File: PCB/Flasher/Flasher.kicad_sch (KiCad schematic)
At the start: 58 parts, among them J1 Reset, J2 Wago, J3 Wago, J4 USB-C-Socket-V, J5 TF_PUSH, U1 ESP32-S3-MINI-1, U2 TPS562246, U3 FT231XQ, U4 TPS22916CNYFPR

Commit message: Started placement
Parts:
- removed FID1, FID2: Fiducial, Fiducial:Fiducial_1mm_Mask2mm, symbol Mechanical:Fiducial
- removed V1, V4: ~, RevK:VCUT70N, symbol RevK:VCUT

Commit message: New tweaks
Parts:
- added D11: XL-1010RGBC-WS2812B, RevK:SMD1010, symbol RevK:WS2812B-1mm
- added U5: TPS22916CNYFPR, RevK:WCSP-4-0.78x0.78, symbol RevK:TPS22916
- C13: footprint RevK:C_0402 -> RevK:C_0201
- J2, J3: footprint RevK:WAGO-2060-453-998-404 -> RevK:WAGO-2060-453-998-404-S
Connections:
- net DC is gone; now on net VBUS: C1.1, C2.1, C3.1, R1.2, U2.1 (VIN)
- net +3.3V: now also D11.2 (+), U5.A2 (VIN)
- net GND: now also D11.3 (-), U5.B1 (GND)
- net LED: now also U1.16 (GPIO12); no longer U1.27 (GPIO47)
- net SDCD: now also U1.12 (GPIO8); no longer U1.22 (GPIO18)
- net SDCLK: now also U1.9 (GPIO5); no longer U1.19 (GPIO15)
- net SDCMD: now also U1.8 (GPIO4); no longer U1.18 (GPIO14)
- net SDDAT0: now also U1.10 (GPIO6); no longer U1.20 (GPIO16)
- net SDDAT1: now also U1.11 (GPIO7); no longer U1.21 (GPIO17)
- net SDDAT2: now also U1.6 (GPIO2); no longer U1.16 (GPIO12)
- net SDDAT3: now also U1.7 (GPIO3); no longer U1.17 (GPIO13)
- net at D10.1 (O): now also D11.4 (I)
- net VOUT: now reaches J3.1 (Pin_1), U4.A1 (VOUT)
- net VOUT: now also U5.A1 (VOUT)
- net PWR3: now reaches U1.13 (GPIO9)
- net PWR3: now also U5.B2 (ON)
- net PWR renamed PWR5
- no-connect marks 27 -> 26

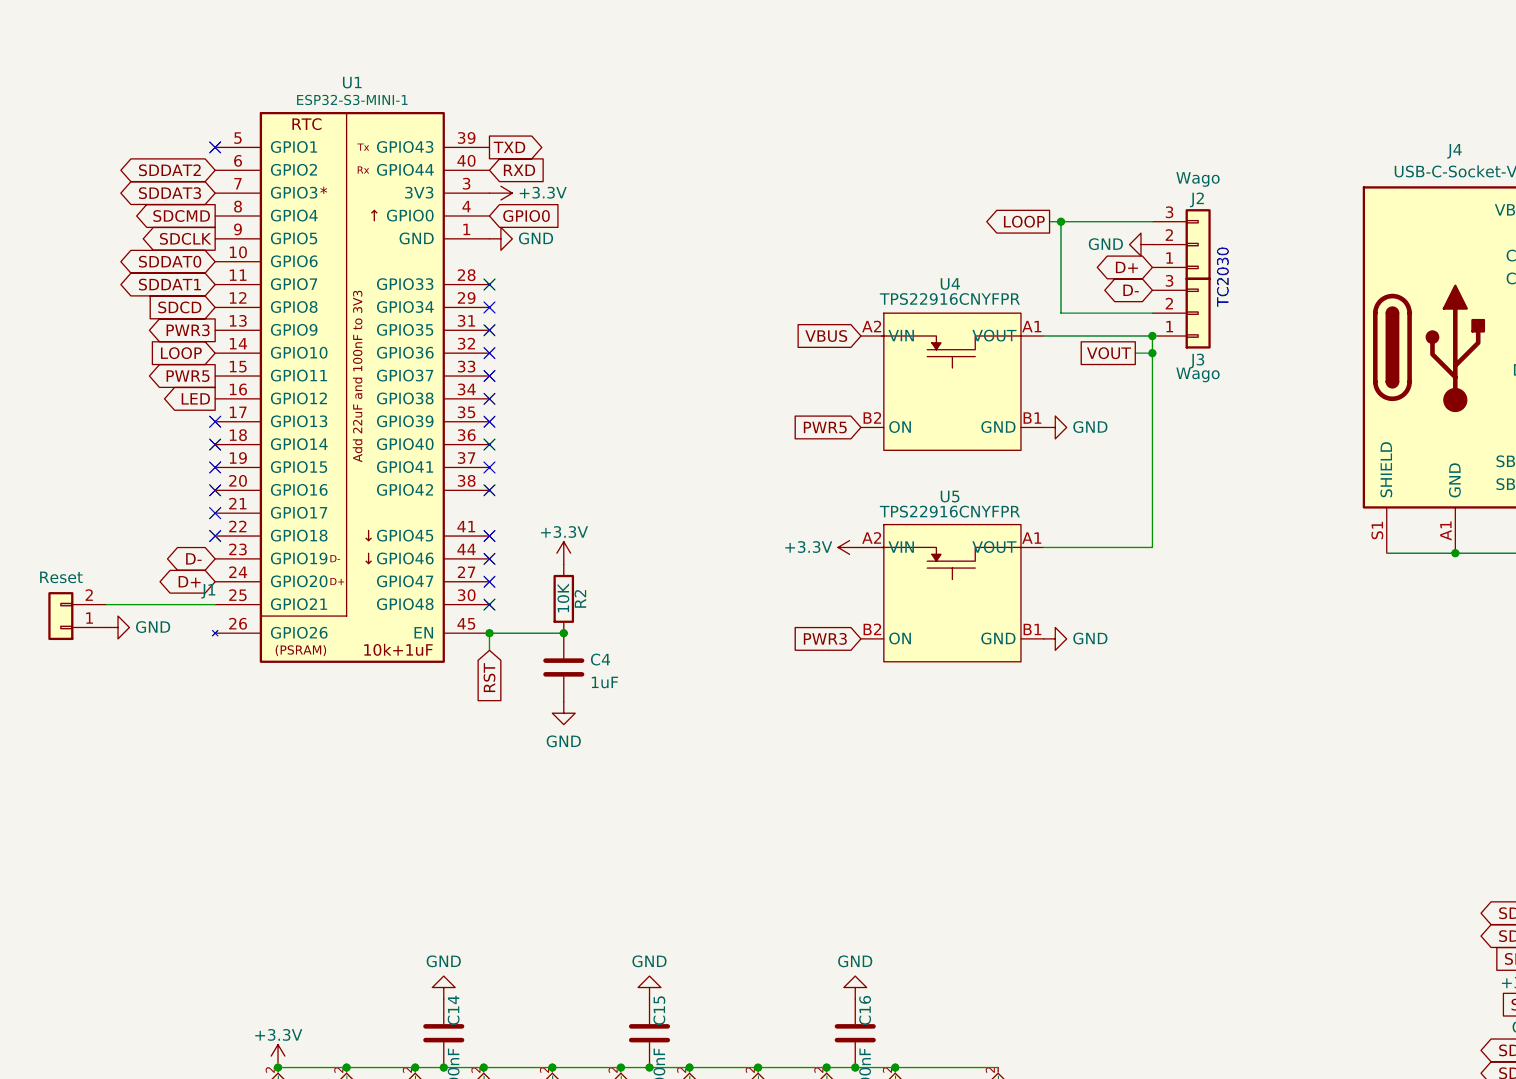
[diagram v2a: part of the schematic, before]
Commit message: New sockets
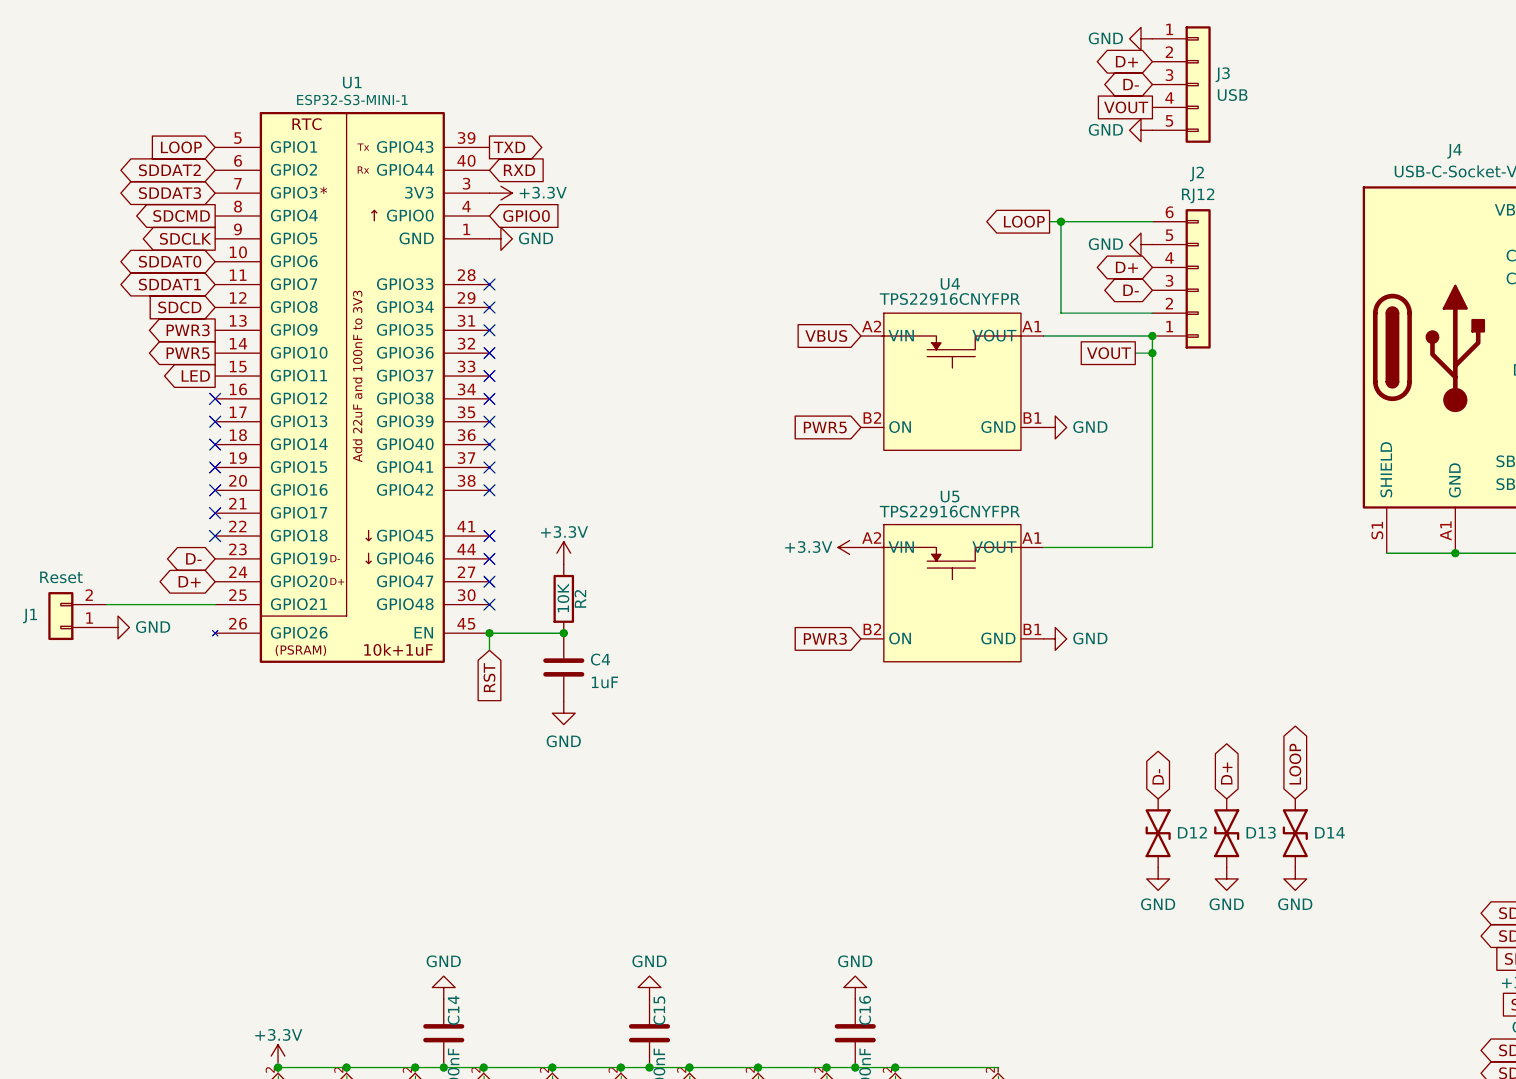
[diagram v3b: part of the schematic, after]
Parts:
- removed J2, J3: Wago, RevK:WAGO-2060-453-998-404-S, symbol Connector_Generic:Conn_01x03
- added D12, D13, D14: ~, RevK:DFN1006-2L, symbol RevK:ES05D1MC10
- added J2: RJ12, RevK:RJ12_Horizontal, symbol Connector_Generic:Conn_01x06
- added J3: USB, RevK:USB_A_Horizontal, symbol Connector_Generic:Conn_01x05
- R10, R9: MPN (none) -> C273295
- R7, R8: MPN (none) -> C270344
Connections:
- net D+: now also D13.2, J2.4 (Pin_4), J3.2 (Pin_2)
- net D-: now also D12.2, J2.3 (Pin_3), J3.3 (Pin_3)
- net GND: now also D12.1, D13.1, D14.1, J2.5 (Pin_5), J3.1 (Pin_1), J3.5 (Pin_5)
- net LED: now also U1.15 (GPIO11); no longer U1.16 (GPIO12)
- net LOOP: now also U1.5 (GPIO1), D14.2, J2.2 (Pin_2), J2.6 (Pin_6); no longer U1.14 (GPIO10)
- net PWR5: now also U1.14 (GPIO10); no longer U1.15 (GPIO11)
- net VOUT: now also J2.1 (Pin_1), J3.4 (Pin_4)
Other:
- note removed: "TC2030"

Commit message: Board ready
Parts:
- added SW1: SW_Push_DPDT, RevK:SW_Push_DPDT, symbol RevK:SW_Push_DPDT
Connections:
- net GND: now also SW1.3 (C)
- net BTN: now reaches U1.16 (GPIO12)
- net BTN: now also SW1.2 (B)
- no-connect marks 26 -> 29
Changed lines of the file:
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@@
 	)
 	(no_connect
+		(at 50.8 101.6)
+	)
+	(no_connect
 		(at 43.815 61.595)
 	)
@@
 	)
 	(no_connect
+		(at 60.96 101.6)
+	)
+	(no_connect
 		(at 43.815 64.135)
 	)
@@
 	)
 	(no_connect
-		(at 74.295 48.895)
+		(at 43.815 59.055)
 	)
 	(no_connect
-		(at 43.815 59.055)
+		(at 66.04 101.6)
 	)
 	(no_connect
@@
 	)
 	(no_connect
-		(at 43.815 56.515)
+		(at 74.295 48.895)
 	)
 	(no_connect
@@
 	)
 	(no_connect
+		(at 63.5 111.76)
+	)
+	(no_connect
 		(at 74.295 56.515)
 	)
@@
 		)
 	)
+	(global_label "BTN"
+		(shape input)
+		(at 43.815 56.515 180)
+		(fields_autoplaced yes)
+		(effects
+			(font
+				(size 1.27 1.27)
+			)
+			(justify right)
+		)
+		(property "Intersheetrefs" "${INTERSHEET_REFS}"
+			(at 37.9159 56.515 0)
+			(effects
+				(font
+					(size 1.27 1.27)
+				)
+				(justify right)
+				(hide yes)
+			)
+		)
+	)
 	(global_label "VOUT"
 		(shape passive)
@@
 		)
 	)
+	(global_label "BTN"
+		(shape output)
+		(at 53.34 111.76 270)
+		(fields_autoplaced yes)
+		(effects
+			(font
+				(size 1.27 1.27)
+			)
+			(justify right)
+		)
+		(property "Intersheetrefs" "${INTERSHEET_REFS}"
+			(at 53.34 117.6591 90)
+			(effects
+				(font
+					(size 1.27 1.27)
+				)
+				(justify right)
+				(hide yes)
+			)
+		)
+	)
 	(global_label "LOOP"
 		(shape bidirectional)
@@
 	)
 	(symbol
+		(lib_id "RevK:SW_Push_DPDT")
+		(at 58.42 106.68 90)
+		(unit 1)
+		(exclude_from_sim no)
+		(in_bom yes)
+		(on_board yes)
+		(dnp no)
+		(fields_autoplaced yes)
+		(property "Reference" "SW1"
+			(at 45.5125 106.68 0)
+			(effects
+				(font
+					(size 1.27 1.27)
+				)
+			)
+		)
+		(property "Value" "SW_Push_DPDT"
+			(at 47.9368 106.68 0)
+			(effects
+				(font
+					(size 1.27 1.27)
+				)
+			)
+		)
+		(property "Footprint" "RevK:SW_Push_DPDT"
+			(at 53.34 106.68 0)
+			(effects
+				(font
+					(size 1.27 1.27)
+				)
+				(hide yes)
+			)
+		)
+		(property "Datasheet" "~"
+			(at 53.34 106.68 0)
+			(effects
+				(font
+					(size 1.27 1.27)
+				)
+				(hide yes)
+			)
+		)
+		(property "Description" "Momentary Switch, dual pole double throw"
+			(at 58.42 106.68 0)
+			(effects
+				(font
+					(size 1.27 1.27)
+				)
+				(hide yes)
+			)
+		)
+		(property "MPN" "C2911139"
+			(at 58.42 106.68 0)
+			(effects
+				(font
+					(size 1.27 1.27)
+				)
+				(hide yes)
+			)
+		)
+		(pin "3"
+		)
+		(pin "6"
+		)
+		(pin "4"
+		)
+		(pin "2"
+		)
+		(pin "5"
+		)
+		(pin "1"
+		)
+		(instances
+			(project "Flasher"
+				(path "/46c350bb-7de4-4e81-aafd-4af55e37aab0"
+					(reference "SW1")
+					(unit 1)
+				)
+			)
+		)
+	)
+	(symbol
 		(lib_id "power:GND")
 		(at 212.09 41.91 0)
@@
 					(unit 1)
 				)
+			)
+		)
+	)
+	(symbol
+		(lib_id "power:GND")
+		(at 55.88 101.6 180)
+		(unit 1)
+		(exclude_from_sim no)
+		(in_bom yes)
+		(on_board yes)
+		(dnp no)
+		(fields_autoplaced yes)
+		(property "Reference" "#PWR032"
+			(at 55.88 95.25 0)
+			(effects
+				(font
+					(size 1.27 1.27)
+				)
+				(hide yes)
+			)
+		)
+		(property "Value" "GND"
+			(at 55.88 97.4669 0)
+			(effects
+				(font
+					(size 1.27 1.27)
+				)
+			)
+		)
+		(property "Footprint" ""
+			(at 55.88 101.6 0)
+			(effects
+				(font
+					(size 1.27 1.27)
+				)
+				(hide yes)
+			)
+		)
+		(property "Datasheet" ""
+			(at 55.88 101.6 0)
+			(effects
+				(font
+					(size 1.27 1.27)
+				)
+				(hide yes)
+			)
+		)
+		(property "Description" "Power symbol creates a global label with name \"GND\" , ground"
+			(at 55.88 101.6 0)
+			(effects
+				(font
+					(size 1.27 1.27)
+				)
+				(hide yes)
+			)
+		)
+		(pin "1"
+		)
+		(instances
+			(project "Flasher"
+				(path "/46c350bb-7de4-4e81-aafd-4af55e37aab0"
+					(reference "#PWR032")
+					(unit 1)
+				)

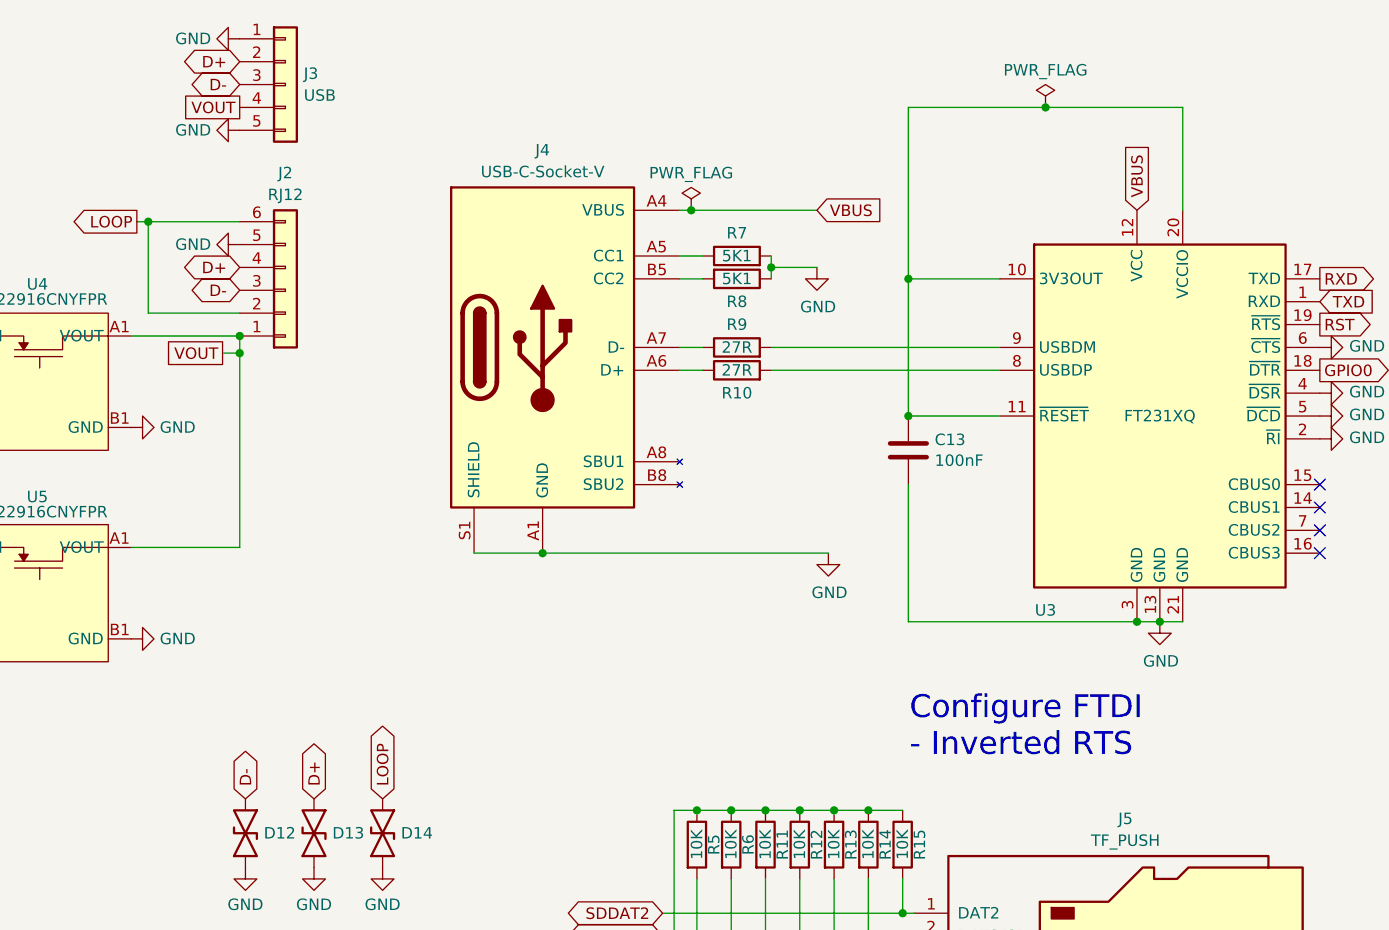
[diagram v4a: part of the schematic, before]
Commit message: Reverse USB, FFS
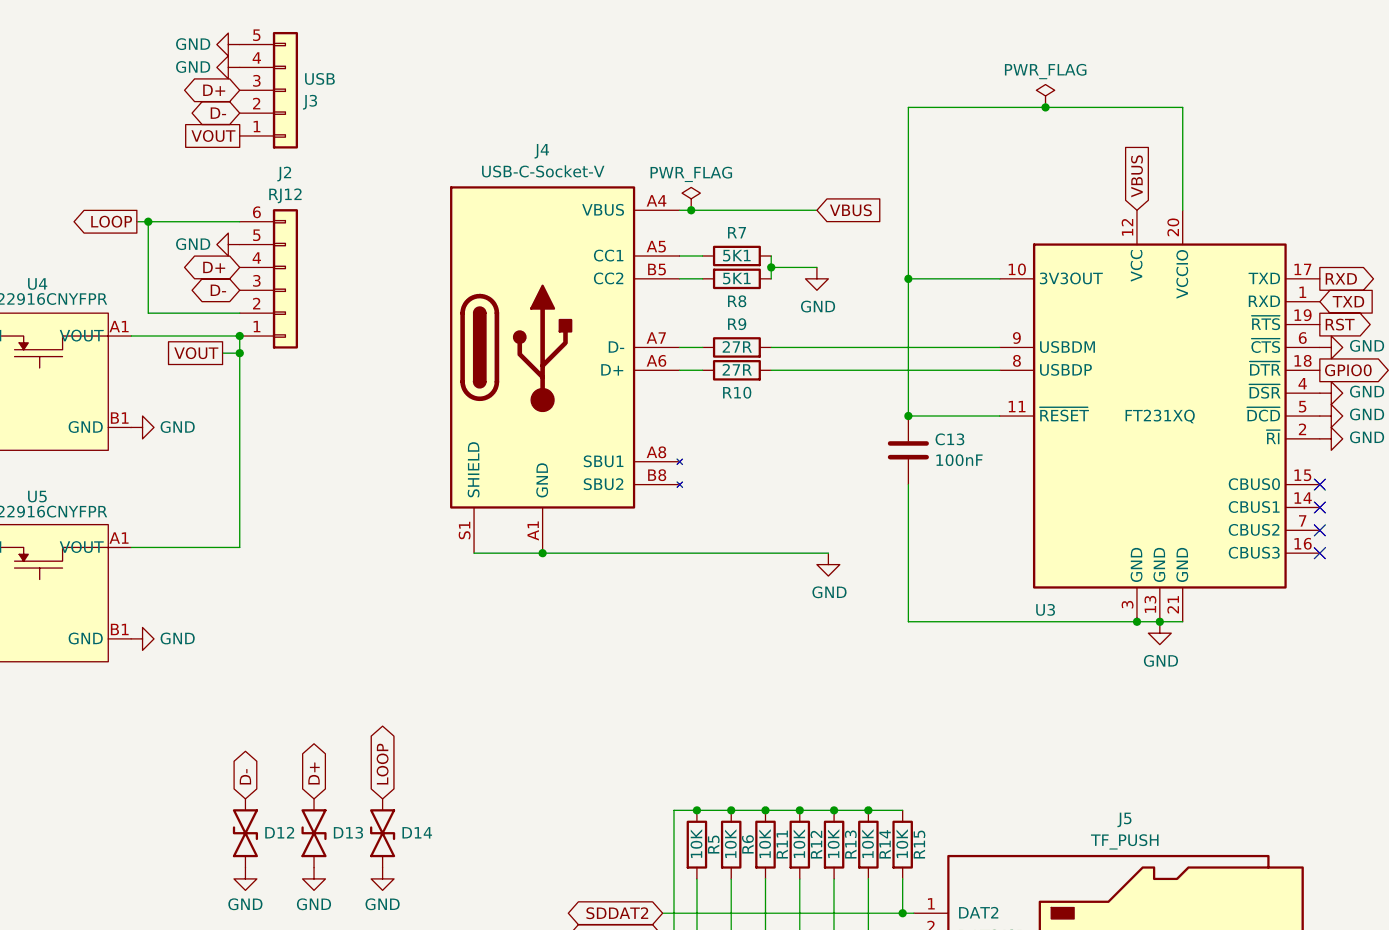
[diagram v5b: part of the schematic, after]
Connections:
- net D+: now also J3.3 (Pin_3); no longer J3.2 (Pin_2)
- net D-: now also J3.2 (Pin_2); no longer J3.3 (Pin_3)
- net GND: now also J3.4 (Pin_4); no longer J3.1 (Pin_1)
- net VOUT: now also J3.1 (Pin_1); no longer J3.4 (Pin_4)
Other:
- note removed: "Configure FTDI - Inverted RTS"
- moved on the sheet: J3
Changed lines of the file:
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@@
 		(comment 2 "www.me.uk")
 	)
-	(text "Configure FTDI\n- Inverted RTS"
-		(exclude_from_sim no)
-		(at 222.377 96.52 0)
-		(effects
-			(font
-				(size 2.54 2.54)
-			)
-			(justify left bottom)
-		)
-	)
 	(junction
 		(at 113.03 176.53)
@@
 	(global_label "D-"
 		(shape bidirectional)
-		(at 147.955 21.59 180)
+		(at 147.955 24.765 180)
 		(fields_autoplaced yes)
 		(effects
@@
 		)
 		(property "Intersheetrefs" "${INTERSHEET_REFS}"
-			(at 141.8291 21.59 0)
+			(at 141.8291 24.765 0)
 			(effects
 				(font
@@
 	(global_label "D+"
 		(shape bidirectional)
-		(at 147.955 19.05 180)
+		(at 147.955 22.225 180)
 		(fields_autoplaced yes)
 		(effects
@@
 		)
 		(property "Intersheetrefs" "${INTERSHEET_REFS}"
-			(at 141.8291 19.05 0)
+			(at 141.8291 22.225 0)
 			(effects
 				(font
@@
 	(global_label "VOUT"
 		(shape passive)
-		(at 147.955 24.13 180)
+		(at 147.955 27.305 180)
 		(fields_autoplaced yes)
 		(effects
@@
 		)
 		(property "Intersheetrefs" "${INTERSHEET_REFS}"
-			(at 141.8593 24.13 0)
+			(at 141.8593 27.305 0)
 			(effects
 				(font
@@
 	(symbol
 		(lib_id "Connector_Generic:Conn_01x05")
-		(at 153.035 21.59 0)
+		(at 153.035 22.225 0)
+		(mirror x)
 		(unit 1)
 		(exclude_from_sim no)
@@
 		(on_board yes)
 		(dnp no)
-		(fields_autoplaced yes)
 		(property "Reference" "J3"
-			(at 155.067 20.3778 0)
+			(at 155.067 23.4372 0)
 			(effects
 				(font
@@
 		)
 		(property "Value" "USB"
-			(at 155.067 22.8021 0)
+			(at 155.067 21.0129 0)
 			(effects
 				(font
@@
 		)
 		(property "Footprint" "RevK:USB_A_Horizontal"
-			(at 153.035 21.59 0)
+			(at 153.035 22.225 0)
 			(effects
 				(font
@@
 		)
 		(property "Datasheet" "~"
-			(at 153.035 21.59 0)
+			(at 153.035 22.225 0)
 			(effects
 				(font
@@
 		)
 		(property "Description" "Generic connector, single row, 01x05, script generated (kicad-library-utils/schlib/autogen/connector/)"
-			(at 153.035 21.59 0)
+			(at 153.035 22.225 0)
 			(effects
 				(font
@@
 		)
 		(property "MPN" "C720525"
-			(at 153.035 21.59 0)
+			(at 153.035 22.225 0)
 			(effects
 				(font
@@
 	(symbol
 		(lib_id "power:GND")
-		(at 147.955 16.51 270)
+		(at 147.955 19.685 270)
 		(unit 1)
 		(exclude_from_sim no)
@@
 		(fields_autoplaced yes)
 		(property "Reference" "#PWR030"
-			(at 141.605 16.51 0)
+			(at 141.605 19.685 0)
 			(effects
 				(font
@@
 		)
 		(property "Value" "GND"
-			(at 144.7801 16.51 90)
+			(at 144.7801 19.685 90)
 			(effects
 				(font
@@
 		)
 		(property "Footprint" ""
-			(at 147.955 16.51 0)
+			(at 147.955 19.685 0)
 			(effects
 				(font
@@
 		)
 		(property "Datasheet" ""
-			(at 147.955 16.51 0)
+			(at 147.955 19.685 0)
 			(effects
 				(font
@@
 		)
 		(property "Description" "Power symbol creates a global label with name \"GND\" , ground"
-			(at 147.955 16.51 0)
+			(at 147.955 19.685 0)
 			(effects
 				(font
@@
 	(symbol
 		(lib_id "power:GND")
-		(at 147.955 26.67 270)
+		(at 147.955 17.145 270)
 		(unit 1)
 		(exclude_from_sim no)
@@
 		(fields_autoplaced yes)
 		(property "Reference" "#PWR031"
-			(at 141.605 26.67 0)
+			(at 141.605 17.145 0)
 			(effects
 				(font
@@
 		)
 		(property "Value" "GND"
-			(at 144.7801 26.67 90)
+			(at 144.7801 17.145 90)
 			(effects
 				(font
@@
 		)
 		(property "Footprint" ""
-			(at 147.955 26.67 0)
+			(at 147.955 17.145 0)
 			(effects
 				(font
@@
 		)
 		(property "Datasheet" ""
-			(at 147.955 26.67 0)
+			(at 147.955 17.145 0)
 			(effects
 				(font
@@
 		)
 		(property "Description" "Power symbol creates a global label with name \"GND\" , ground"
-			(at 147.955 26.67 0)
+			(at 147.955 17.145 0)
 			(effects
 				(font

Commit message: PCB update
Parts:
- added C17, C35: 220uF Tant, RevK:CP_EIA-3528-21_Kemet-B, symbol Device:C_Polarized
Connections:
- net +3.3V: now also C35.1
- net GND: now also C17.2, C35.2
- net VBUS: now also C17.1
